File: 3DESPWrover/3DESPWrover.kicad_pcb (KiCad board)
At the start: 2 copper layers, 48.3 x 48.3 mm, 30 parts, among them J1 Conn_01x04_Male, J3 Conn_02x03_Odd_Even, J4 Conn_02x07_Odd_Even, SW1 SW_Push, SW2 SW_Push, U1 ESP32-S2-WROVER, U2 K78xxJT-500R3

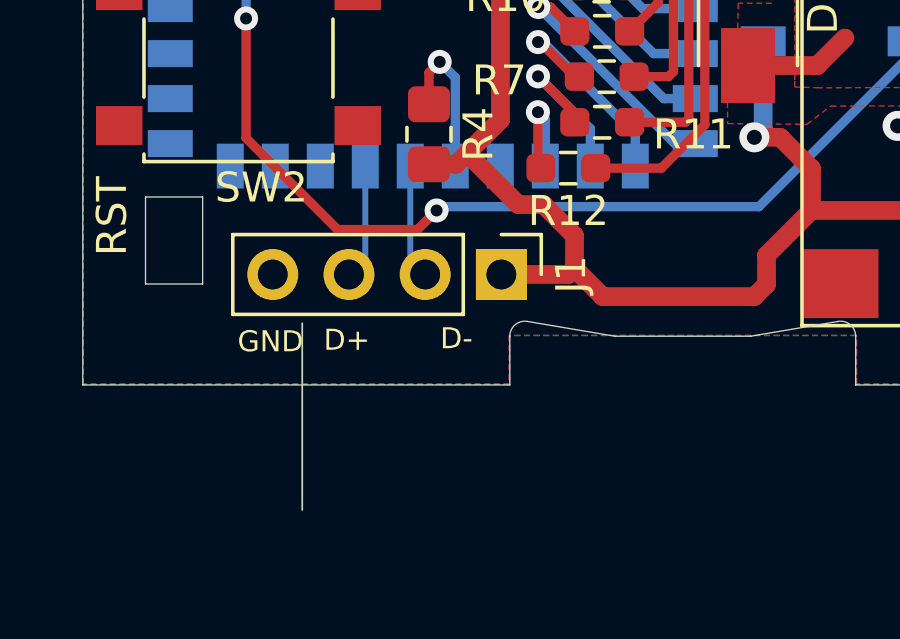
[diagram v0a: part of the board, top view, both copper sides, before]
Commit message: Sent cube to assembly manufacture, soldered PressureSensors, created test sketch for pressure sensors for arduino uno
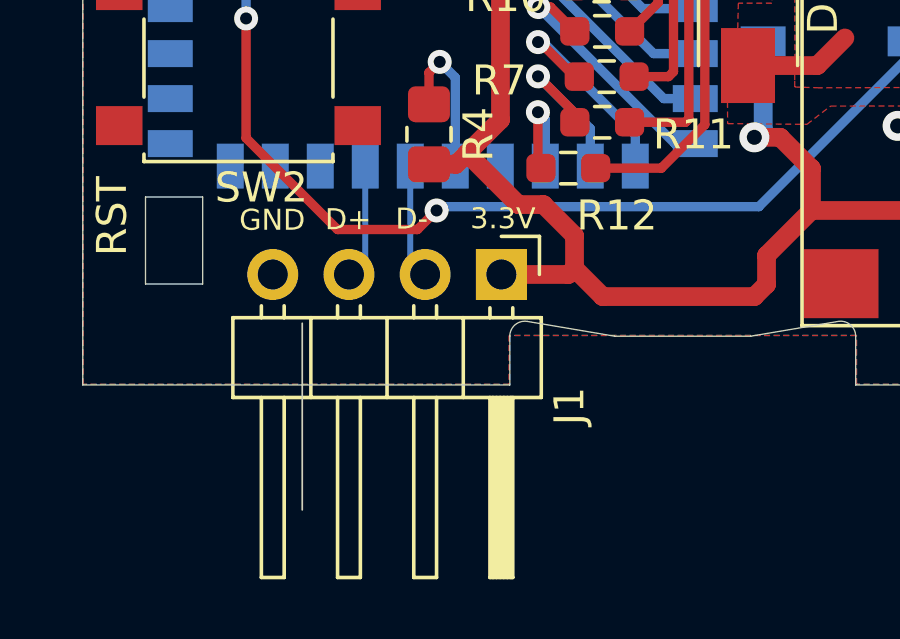
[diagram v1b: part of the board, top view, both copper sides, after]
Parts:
- J1: footprint Connector_PinHeader_2.54mm:PinHeader_1x04_P2.54mm_Vertical -> Connector_PinHeader_2.54mm:PinHeader_1x04_P2.54mm_Horizontal
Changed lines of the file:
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@@
     )
   )
-  (footprint "Connector_PinHeader_2.54mm:PinHeader_1x04_P2.54mm_Vertical" (layer "F.Cu")
+  (footprint "Connector_PinHeader_2.54mm:PinHeader_1x04_P2.54mm_Horizontal" (layer "F.Cu")
     (at 213.868 86.3346 -90)
-    (descr "Through hole straight pin header, 1x04, 2.54mm pitch, single row")
-    (tags "Through hole pin header THT 1x04 2.54mm single row")
+    (descr "Through hole angled pin header, 1x04, 2.54mm pitch, 6mm pin length, single row")
+    (tags "Through hole angled pin header THT 1x04 2.54mm single row")
     (property "Sheetfile" "3DESPWrover.kicad_sch")
     (property "Sheetname" "")
     (attr through_hole)
-    (fp_text reference "J1" (at 0 -2.33 90) (layer "F.SilkS")
-      (effects (font (size 1 1) (thickness 0.15)))
-    )
-    (fp_text value "Conn_01x04_Male" (at 0 9.95 90) (layer "F.Fab")
-      (effects (font (size 1 1) (thickness 0.15)))
-    )
-    (fp_text user "${REFERENCE}" (at 0 3.81) (layer "F.Fab")
-      (effects (font (size 1 1) (thickness 0.15)))
-    )
-    (fp_line (start -1.33 8.95) (end 1.33 8.95) (layer "F.SilkS") (width 0.12))
-    (fp_line (start -1.33 1.27) (end 1.33 1.27) (layer "F.SilkS") (width 0.12))
-    (fp_line (start -1.33 1.27) (end -1.33 8.95) (layer "F.SilkS") (width 0.12))
-    (fp_line (start 1.33 1.27) (end 1.33 8.95) (layer "F.SilkS") (width 0.12))
-    (fp_line (start -1.33 -1.33) (end 0 -1.33) (layer "F.SilkS") (width 0.12))
-    (fp_line (start -1.33 0) (end -1.33 -1.33) (layer "F.SilkS") (width 0.12))
-    (fp_line (start -1.8 9.4) (end 1.8 9.4) (layer "F.CrtYd") (width 0.05))
+    (fp_text reference "J1" (at 4.385 -2.27 -90) (layer "F.SilkS")
+      (effects (font (size 1 1) (thickness 0.15)))
+    )
+    (fp_text value "Conn_01x04_Male" (at 4.385 9.89 -90) (layer "F.Fab")
+      (effects (font (size 1 1) (thickness 0.15)))
+    )
+    (fp_text user "${REFERENCE}" (at 2.77 3.81) (layer "F.Fab")
+      (effects (font (size 1 1) (thickness 0.15)))
+    )
+    (fp_line (start 1.44 3.81) (end 4.1 3.81) (layer "F.SilkS") (width 0.12))
+    (fp_line (start 10.1 2.92) (end 4.1 2.92) (layer "F.SilkS") (width 0.12))
+    (fp_line (start 4.1 -0.38) (end 10.1 -0.38) (layer "F.SilkS") (width 0.12))
+    (fp_line (start 10.1 2.16) (end 10.1 2.92) (layer "F.SilkS") (width 0.12))
+    (fp_line (start 1.042929 8) (end 1.44 8) (layer "F.SilkS") (width 0.12))
+    (fp_line (start 10.1 -0.38) (end 10.1 0.38) (layer "F.SilkS") (width 0.12))
+    (fp_line (start 1.042929 2.92) (end 1.44 2.92) (layer "F.SilkS") (width 0.12))
+    (fp_line (start 1.44 1.27) (end 4.1 1.27) (layer "F.SilkS") (width 0.12))
+    (fp_line (start 4.1 2.16) (end 10.1 2.16) (layer "F.SilkS") (width 0.12))
+    (fp_line (start 10.1 5.46) (end 4.1 5.46) (layer "F.SilkS") (width 0.12))
+    (fp_line (start 4.1 0.04) (end 10.1 0.04) (layer "F.SilkS") (width 0.12))
+    (fp_line (start 4.1 0.16) (end 10.1 0.16) (layer "F.SilkS") (width 0.12))
+    (fp_line (start 4.1 7.24) (end 10.1 7.24) (layer "F.SilkS") (width 0.12))
+    (fp_line (start 1.042929 7.24) (end 1.44 7.24) (layer "F.SilkS") (width 0.12))
+    (fp_line (start -1.27 0) (end -1.27 -1.27) (layer "F.SilkS") (width 0.12))
+    (fp_line (start 1.11 0.38) (end 1.44 0.38) (layer "F.SilkS") (width 0.12))
+    (fp_line (start 1.44 6.35) (end 4.1 6.35) (layer "F.SilkS") (width 0.12))
+    (fp_line (start 1.042929 4.7) (end 1.44 4.7) (layer "F.SilkS") (width 0.12))
+    (fp_line (start 1.042929 5.46) (end 1.44 5.46) (layer "F.SilkS") (width 0.12))
+    (fp_line (start -1.27 -1.27) (end 0 -1.27) (layer "F.SilkS") (width 0.12))
+    (fp_line (start 4.1 -0.08) (end 10.1 -0.08) (layer "F.SilkS") (width 0.12))
+    (fp_line (start 1.44 8.95) (end 4.1 8.95) (layer "F.SilkS") (width 0.12))
+    (fp_line (start 1.44 -1.33) (end 1.44 8.95) (layer "F.SilkS") (width 0.12))
+    (fp_line (start 10.1 7.24) (end 10.1 8) (layer "F.SilkS") (width 0.12))
+    (fp_line (start 4.1 -0.2) (end 10.1 -0.2) (layer "F.SilkS") (width 0.12))
+    (fp_line (start 4.1 4.7) (end 10.1 4.7) (layer "F.SilkS") (width 0.12))
+    (fp_line (start 4.1 -1.33) (end 1.44 -1.33) (layer "F.SilkS") (width 0.12))
+    (fp_line (start 10.1 0.38) (end 4.1 0.38) (layer "F.SilkS") (width 0.12))
+    (fp_line (start 4.1 -0.32) (end 10.1 -0.32) (layer "F.SilkS") (width 0.12))
+    (fp_line (start 1.042929 2.16) (end 1.44 2.16) (layer "F.SilkS") (width 0.12))
+    (fp_line (start 1.11 -0.38) (end 1.44 -0.38) (layer "F.SilkS") (width 0.12))
+    (fp_line (start 4.1 8.95) (end 4.1 -1.33) (layer "F.SilkS") (width 0.12))
+    (fp_line (start 10.1 4.7) (end 10.1 5.46) (layer "F.SilkS") (width 0.12))
+    (fp_line (start 4.1 0.28) (end 10.1 0.28) (layer "F.SilkS") (width 0.12))
+    (fp_line (start 10.1 8) (end 4.1 8) (layer "F.SilkS") (width 0.12))
     (fp_line (start -1.8 -1.8) (end -1.8 9.4) (layer "F.CrtYd") (width 0.05))
-    (fp_line (start 1.8 9.4) (end 1.8 -1.8) (layer "F.CrtYd") (width 0.05))
-    (fp_line (start 1.8 -1.8) (end -1.8 -1.8) (layer "F.CrtYd") (width 0.05))
-    (fp_line (start -1.27 8.89) (end -1.27 -0.635) (layer "F.Fab") (width 0.1))
-    (fp_line (start -0.635 -1.27) (end 1.27 -1.27) (layer "F.Fab") (width 0.1))
-    (fp_line (start 1.27 8.89) (end -1.27 8.89) (layer "F.Fab") (width 0.1))
-    (fp_line (start 1.27 -1.27) (end 1.27 8.89) (layer "F.Fab") (width 0.1))
-    (fp_line (start -1.27 -0.635) (end -0.635 -1.27) (layer "F.Fab") (width 0.1))
+    (fp_line (start -1.8 9.4) (end 10.55 9.4) (layer "F.CrtYd") (width 0.05))
+    (fp_line (start 10.55 -1.8) (end -1.8 -1.8) (layer "F.CrtYd") (width 0.05))
+    (fp_line (start 10.55 9.4) (end 10.55 -1.8) (layer "F.CrtYd") (width 0.05))
+    (fp_line (start -0.32 2.22) (end 1.5 2.22) (layer "F.Fab") (width 0.1))
+    (fp_line (start 4.04 7.94) (end 10.04 7.94) (layer "F.Fab") (width 0.1))
+    (fp_line (start 1.5 8.89) (end 1.5 -0.635) (layer "F.Fab") (width 0.1))
+    (fp_line (start -0.32 -0.32) (end 1.5 -0.32) (layer "F.Fab") (width 0.1))
+    (fp_line (start -0.32 7.94) (end 1.5 7.94) (layer "F.Fab") (width 0.1))
+    (fp_line (start 10.04 7.3) (end 10.04 7.94) (layer "F.Fab") (width 0.1))
+    (fp_line (start -0.32 7.3) (end 1.5 7.3) (layer "F.Fab") (width 0.1))
+    (fp_line (start 4.04 -1.27) (end 4.04 8.89) (layer "F.Fab") (width 0.1))
+    (fp_line (start -0.32 2.22) (end -0.32 2.86) (layer "F.Fab") (width 0.1))
+    (fp_line (start 4.04 2.22) (end 10.04 2.22) (layer "F.Fab") (width 0.1))
+    (fp_line (start -0.32 0.32) (end 1.5 0.32) (layer "F.Fab") (width 0.1))
+    (fp_line (start 2.135 -1.27) (end 4.04 -1.27) (layer "F.Fab") (width 0.1))
+    (fp_line (start 10.04 4.76) (end 10.04 5.4) (layer "F.Fab") (width 0.1))
+    (fp_line (start 4.04 -0.32) (end 10.04 -0.32) (layer "F.Fab") (width 0.1))
+    (fp_line (start -0.32 4.76) (end 1.5 4.76) (layer "F.Fab") (width 0.1))
+    (fp_line (start 10.04 2.22) (end 10.04 2.86) (layer "F.Fab") (width 0.1))
+    (fp_line (start 4.04 0.32) (end 10.04 0.32) (layer "F.Fab") (width 0.1))
+    (fp_line (start 4.04 7.3) (end 10.04 7.3) (layer "F.Fab") (width 0.1))
+    (fp_line (start -0.32 5.4) (end 1.5 5.4) (layer "F.Fab") (width 0.1))
+    (fp_line (start 4.04 5.4) (end 10.04 5.4) (layer "F.Fab") (width 0.1))
+    (fp_line (start -0.32 7.3) (end -0.32 7.94) (layer "F.Fab") (width 0.1))
+    (fp_line (start 4.04 8.89) (end 1.5 8.89) (layer "F.Fab") (width 0.1))
+    (fp_line (start 1.5 -0.635) (end 2.135 -1.27) (layer "F.Fab") (width 0.1))
+    (fp_line (start -0.32 4.76) (end -0.32 5.4) (layer "F.Fab") (width 0.1))
+    (fp_line (start 4.04 2.86) (end 10.04 2.86) (layer "F.Fab") (width 0.1))
+    (fp_line (start 4.04 4.76) (end 10.04 4.76) (layer "F.Fab") (width 0.1))
+    (fp_line (start -0.32 -0.32) (end -0.32 0.32) (layer "F.Fab") (width 0.1))
+    (fp_line (start -0.32 2.86) (end 1.5 2.86) (layer "F.Fab") (width 0.1))
+    (fp_line (start 10.04 -0.32) (end 10.04 0.32) (layer "F.Fab") (width 0.1))
     (pad "1" thru_hole rect (at 0 0 270) (size 1.7 1.7) (drill 1) (layers *.Cu *.Mask)
       (net 1 "+3V3") (pinfunction "Pin_1") (pintype "passive"))
@@
     (pad "4" thru_hole oval (at 0 7.62 270) (size 1.7 1.7) (drill 1) (layers *.Cu *.Mask)
       (net 2 "GND") (pinfunction "Pin_4") (pintype "passive"))
-    (model "${KICAD6_3DMODEL_DIR}/Connector_PinHeader_2.54mm.3dshapes/PinHeader_1x04_P2.54mm_Vertical.wrl"
+    (model "${KICAD6_3DMODEL_DIR}/Connector_PinHeader_2.54mm.3dshapes/PinHeader_1x04_P2.54mm_Horizontal.wrl"
       (offset (xyz 0 0 0))
       (scale (xyz 1 1 1))
@@
     (property "Sheetname" "")
     (attr smd)
-    (fp_text reference "R12" (at 0 -1.43) (layer "F.SilkS")
+    (fp_text reference "R12" (at -1.62 -1.58) (layer "F.SilkS")
       (effects (font (size 1 1) (thickness 0.15)))
     )
@@
     (effects (font (size 0.7 0.7) (thickness 0.15)))
   )
-  (gr_text "D+" (at 208.7118 88.519) (layer "F.SilkS")
-    (effects (font (size 0.7 0.7) (thickness 0.15)))
-  )
-  (gr_text "D-" (at 212.3694 88.4682) (layer "F.SilkS")
+  (gr_text "D+" (at 208.76 84.5) (layer "F.SilkS")
+    (effects (font (size 0.7 0.7) (thickness 0.15)))
+  )
+  (gr_text "D-" (at 210.88 84.48) (layer "F.SilkS")
     (effects (font (size 0.7 0.7) (thickness 0.15)))
   )
@@
     (effects (font (size 1 1) (thickness 0.15)) (justify left))
   )
+  (gr_text "3.3V" (at 213.92 84.47) (layer "F.SilkS")
+    (effects (font (size 0.7 0.7) (thickness 0.15)))
+  )
   (gr_text "3.3V" (at 238.3 86.62 90) (layer "F.SilkS")
     (effects (font (size 0.7 0.7) (thickness 0.15)))
@@
     (effects (font (size 0.7 0.7) (thickness 0.15)))
   )
-  (gr_text "GND" (at 206.1718 88.5698) (layer "F.SilkS")
-    (effects (font (size 0.7 0.7) (thickness 0.15)))
-  )
+  (gr_text "GND" (at 206.23 84.52) (layer "F.SilkS")
+    (effects (font (size 0.7 0.7) (thickness 0.15)))
+  )
